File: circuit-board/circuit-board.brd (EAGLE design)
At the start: 50.8 x 45.7 mm, 53 parts, among them IC1 UA78M05DCY, Q1 BC547B, Q2 BC547B, U1 MAX3232, U2 ATMEGA328P, U3 ADUM1201BRZ, Y2 16MHz

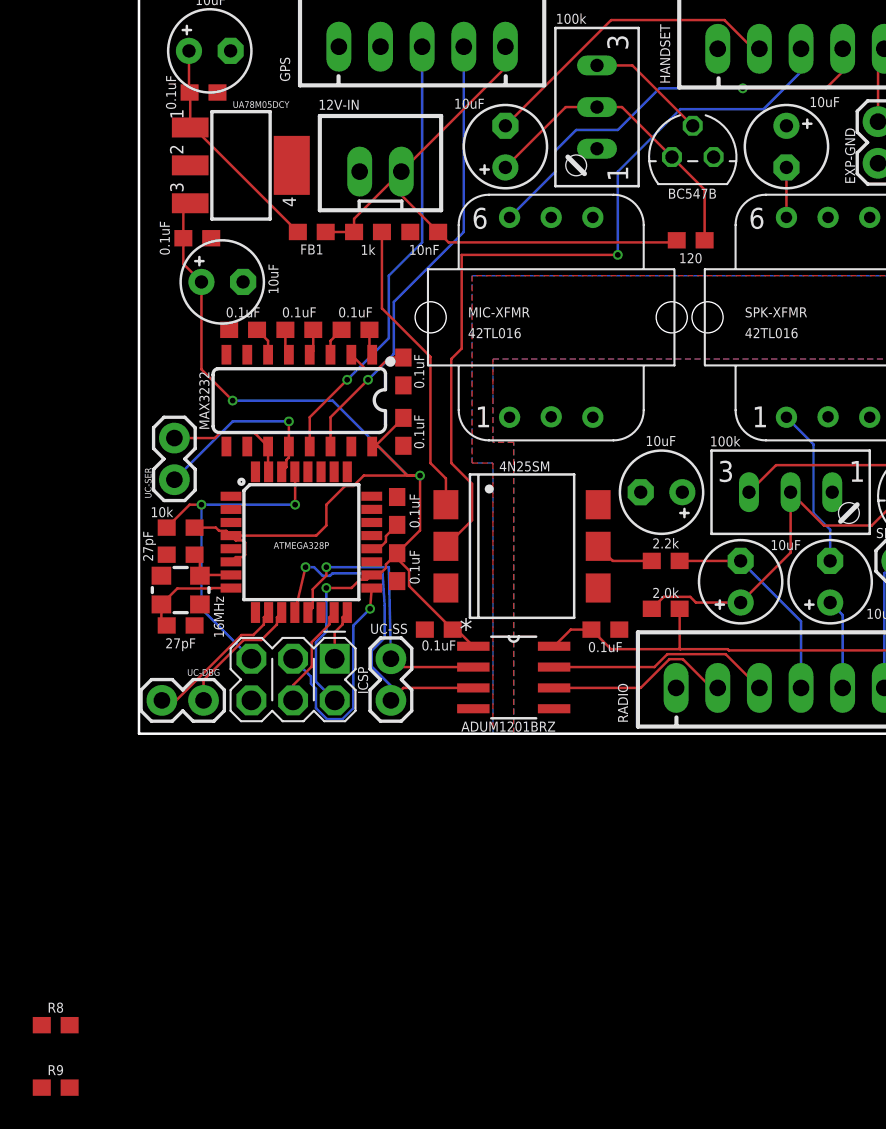
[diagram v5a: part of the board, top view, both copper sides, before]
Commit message: Route new connections for amplifier input resistors
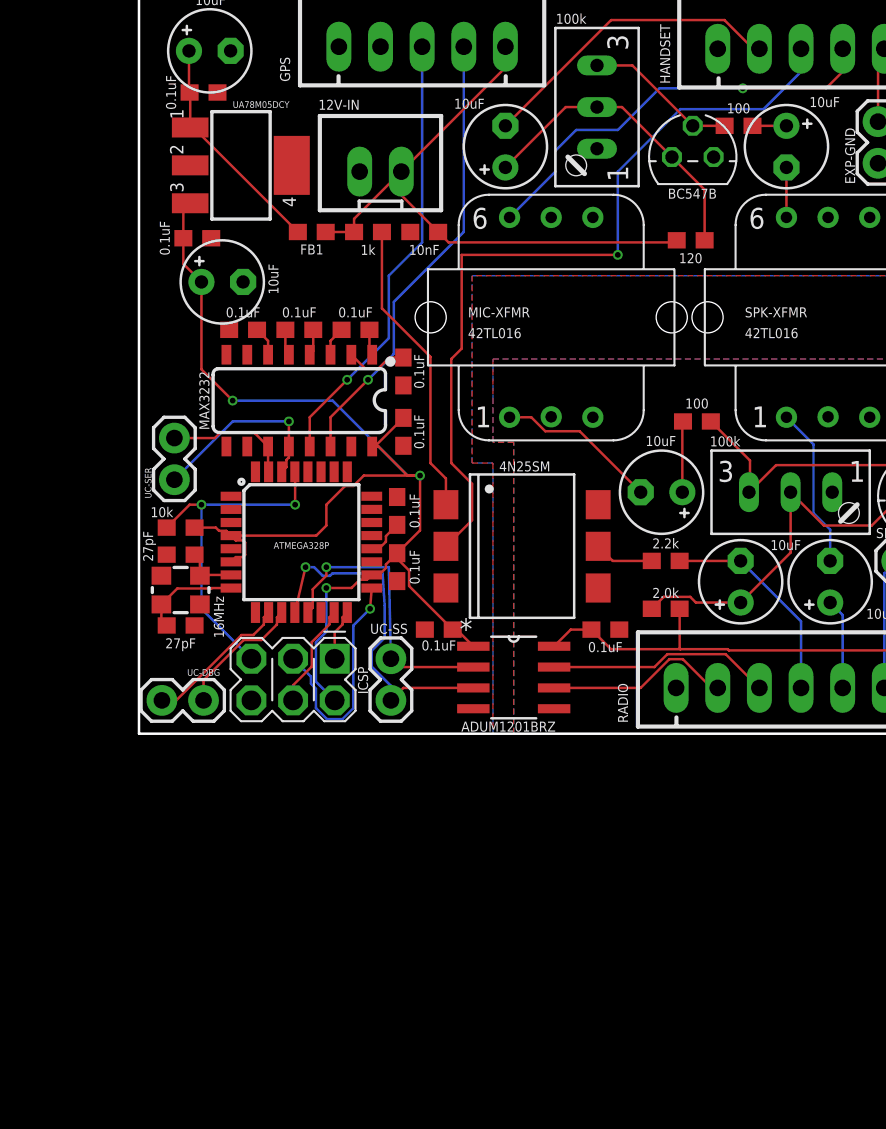
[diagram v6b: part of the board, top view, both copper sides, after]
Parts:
- moved R9 72.0 mm to (36.6, 37.1), turned to 180 degrees
- moved R8 53.7 mm to (34.0, 19.1)
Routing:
- net N$7: track 0.00 -> 9.89 mm
- net N$4: track 11.2 -> 16.5 mm
- net N$8: track 0.00 -> 4.33 mm
- net N$10: track 0.00 -> 2.07 mm
- net N$5: track 7.37 -> 9.31 mm
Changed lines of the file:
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@@
 <attribute name="VALUE" x="13.97" y="29.21" size="0.6096" layer="25" font="vector" ratio="20" rot="R180" align="top-center"/>
 </element>
-<element name="R8" library="SparkFun-Resistors" library_urn="urn:adsk.eagle:library:532" package="0603" package3d_urn="urn:adsk.eagle:package:39650/1" value="100" x="-5.08" y="-17.78">
-<attribute name="PROD_ID" value="RES-07863" x="-5.08" y="-17.78" size="1.778" layer="27" display="off"/>
+<element name="R8" library="SparkFun-Resistors" library_urn="urn:adsk.eagle:library:532" package="0603" package3d_urn="urn:adsk.eagle:package:39650/1" value="100" x="34.036" y="19.05" smashed="yes">
+<attribute name="PROD_ID" value="RES-07863" x="34.036" y="19.05" size="1.778" layer="27" display="off"/>
+<attribute name="VALUE" x="34.036" y="20.447" size="0.6096" layer="25" font="vector" ratio="20" align="top-center"/>
 </element>
-<element name="R9" library="SparkFun-Resistors" library_urn="urn:adsk.eagle:library:532" package="0603" package3d_urn="urn:adsk.eagle:package:39650/1" value="100" x="-5.08" y="-21.59">
-<attribute name="PROD_ID" value="RES-07863" x="-5.08" y="-21.59" size="1.778" layer="27" display="off"/>
+<element name="R9" library="SparkFun-Resistors" library_urn="urn:adsk.eagle:library:532" package="0603" package3d_urn="urn:adsk.eagle:package:39650/1" value="100" x="36.576" y="37.084" smashed="yes" rot="R180">
+<attribute name="PROD_ID" value="RES-07863" x="36.576" y="37.084" size="1.778" layer="27" rot="R180" display="off"/>
+<attribute name="VALUE" x="36.576" y="37.846" size="0.6096" layer="25" font="vector" ratio="20" rot="R180" align="top-center"/>
 </element>
 </elements>
@@
 <contactref element="R10" pad="E"/>
 <wire x1="47.752" y1="16.383" x2="38.862" y2="16.383" width="0.1524" layer="1"/>
-<wire x1="38.862" y1="16.383" x2="37.211" y2="14.732" width="0.1524" layer="1"/>
+<wire x1="38.862" y1="16.383" x2="37.2745" y2="14.7955" width="0.1524" layer="1"/>
 <contactref element="R8" pad="2"/>
-<wire x1="-4.23" y1="-17.78" x2="37.211" y2="14.732" width="0" layer="19" extent="1-1"/>
+<wire x1="37.2745" y1="14.7955" x2="37.211" y2="14.732" width="0.1524" layer="1"/>
+<wire x1="34.886" y1="19.05" x2="37.2745" y2="16.6615" width="0.1524" layer="1"/>
+<wire x1="37.2745" y1="16.6615" x2="37.2745" y2="14.7955" width="0.1524" layer="1"/>
 </signal>
 <signal name="+5V">
@@
 <wire x1="30.099" y1="40.767" x2="27.94" y2="40.767" width="0.1524" layer="1"/>
 <contactref element="R9" pad="2"/>
-<wire x1="-4.23" y1="-21.59" x2="33.782" y2="37.084" width="0" layer="19" extent="1-1"/>
+<wire x1="33.782" y1="37.084" x2="35.726" y2="37.084" width="0.1524" layer="1"/>
 </signal>
 <signal name="N$6">
@@
 <contactref element="MIC-XFMR" pad="1"/>
 <contactref element="C5" pad="-"/>
-<wire x1="22.606" y1="19.304" x2="30.607" y2="14.732" width="0" layer="19" extent="1-1"/>
+<wire x1="23.93136875" y1="19.304" x2="22.606" y2="19.304" width="0.1524" layer="1"/>
+<wire x1="24.78206875" y1="18.4533" x2="23.93136875" y2="19.304" width="0.1524" layer="1"/>
+<wire x1="30.607" y1="14.732" x2="26.8857" y2="18.4533" width="0.1524" layer="1"/>
+<wire x1="26.8857" y1="18.4533" x2="24.78206875" y2="18.4533" width="0.1524" layer="1"/>
 </signal>
 <signal name="N$8">
 <contactref element="C5" pad="+"/>
 <contactref element="R8" pad="1"/>
-<wire x1="-5.93" y1="-17.78" x2="33.147" y2="14.732" width="0" layer="19" extent="1-1"/>
+<wire x1="33.147" y1="14.732" x2="33.147" y2="19.011" width="0.1524" layer="1"/>
+<wire x1="33.147" y1="19.011" x2="33.186" y2="19.05" width="0.1524" layer="1"/>
 </signal>
 <signal name="N$10">
 <contactref element="C2" pad="+"/>
 <contactref element="R9" pad="1"/>
-<wire x1="-5.93" y1="-21.59" x2="39.497" y2="37.084" width="0" layer="19" extent="1-1"/>
+<wire x1="37.426" y1="37.084" x2="39.497" y2="37.084" width="0.1524" layer="1"/>
 </signal>
 </signals>
